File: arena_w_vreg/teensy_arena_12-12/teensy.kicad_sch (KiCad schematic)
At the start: 1 part, among them U13 Teensy4.1

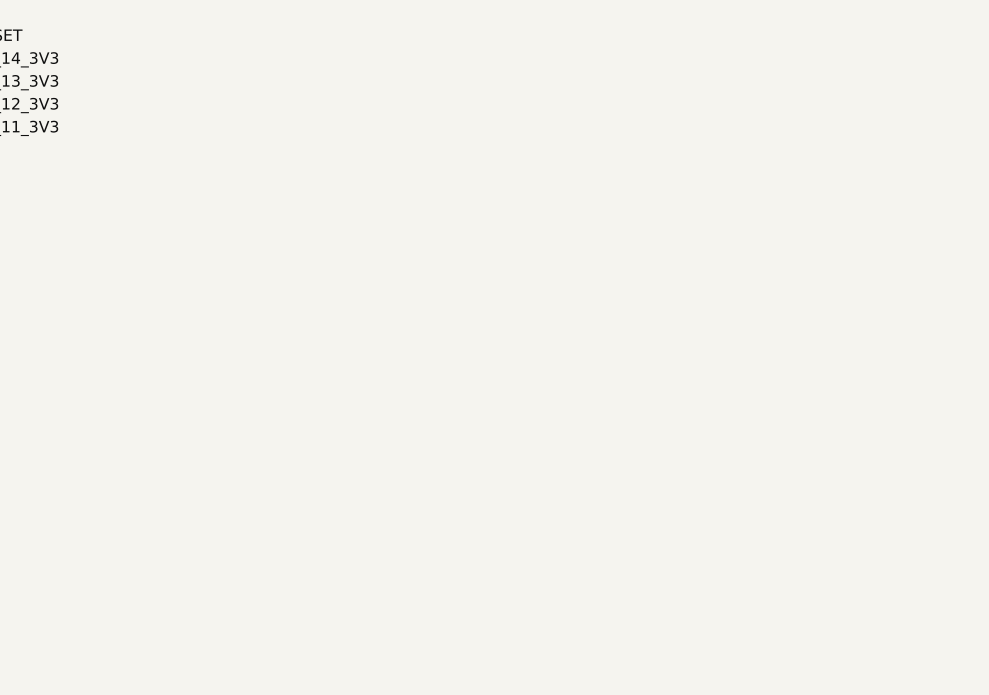
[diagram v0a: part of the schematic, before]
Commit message: Worked on 12-12 teensy arena with voltage regulator.
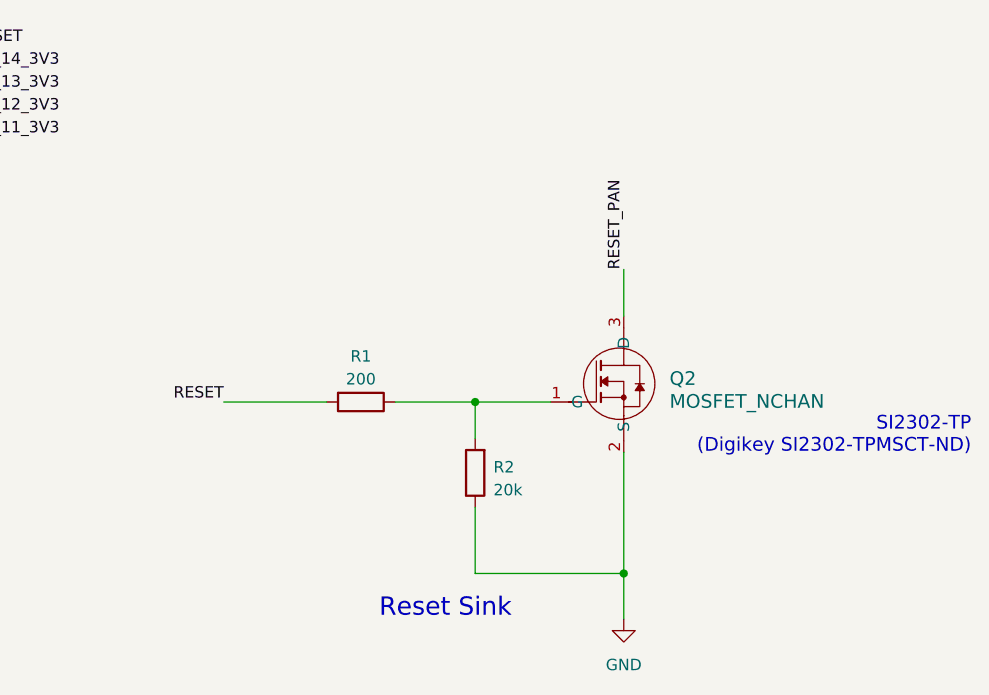
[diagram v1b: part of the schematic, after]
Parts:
- added Q2: MOSFET_NCHAN, Package_TO_SOT_SMD:SOT-23-3, symbol arena_custom:MOSFET_NCHAN
- added R1: 200, Resistor_SMD:R_0805_2012Metric, symbol Device:R
- added R2: 20k, Resistor_SMD:R_0805_2012Metric, symbol Device:R
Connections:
- net GND: now also Q2.2 (S), R2.1
- net RESET: now also R1.2
- new net: Q2.1 (G), R1.1, R2.2
- new net RESET_PAN: Q2.3 (D)
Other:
- note added: "Reset Sink"
- note added: "SI2302-TP (Digikey SI2302-TPMSCT-ND)"
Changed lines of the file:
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@@
 (kicad_sch (version 20230121) (generator eeschema)
   (paper "A4")
+  (junction (at 241.427 145.923) (diameter 0) (color 0 0 0 0)
+  )
+  (junction (at 224.917 126.873) (diameter 0) (color 0 0 0 0)
+  )
   (no_connect (at 165.227 113.919))
   (no_connect (at 165.227 84.709))
@@
     (stroke (width 0) (type default))
   )
+  (wire (pts (xy 196.977 126.873) (xy 208.407 126.873))
+    (stroke (width 0) (type default))
+  )
+  (wire (pts (xy 224.917 145.923) (xy 241.427 145.923))
+    (stroke (width 0) (type default))
+  )
   (wire (pts (xy 105.537 51.689) (xy 109.347 51.689))
     (stroke (width 0) (type default))
@@
     (stroke (width 0) (type default))
   )
+  (wire (pts (xy 224.917 126.873) (xy 233.299 126.873))
+    (stroke (width 0) (type default))
+  )
   (wire (pts (xy 188.087 41.529) (xy 188.087 42.799))
     (stroke (width 0) (type default))
@@
     (stroke (width 0) (type default))
   )
+  (wire (pts (xy 241.427 145.923) (xy 241.427 151.003))
+    (stroke (width 0) (type default))
+  )
   (wire (pts (xy 165.227 56.769) (xy 169.037 56.769))
     (stroke (width 0) (type default))
@@
     (stroke (width 0) (type default))
   )
+  (wire (pts (xy 216.027 126.873) (xy 224.917 126.873))
+    (stroke (width 0) (type default))
+  )
   (wire (pts (xy 105.537 56.769) (xy 109.347 56.769))
     (stroke (width 0) (type default))
@@
     (stroke (width 0) (type default))
   )
+  (wire (pts (xy 241.427 117.348) (xy 241.427 112.141))
+    (stroke (width 0) (type default))
+  )
   (wire (pts (xy 105.537 49.149) (xy 109.347 49.149))
     (stroke (width 0) (type default))
   )
+  (wire (pts (xy 241.427 132.461) (xy 241.427 145.923))
+    (stroke (width 0) (type default))
+  )
   (wire (pts (xy 105.537 92.329) (xy 109.347 92.329))
     (stroke (width 0) (type default))
@@
     (stroke (width 0) (type default))
   )
+  (wire (pts (xy 224.917 126.873) (xy 224.917 130.937))
+    (stroke (width 0) (type default))
+  )
   (wire (pts (xy 165.227 35.179) (xy 169.037 35.179))
     (stroke (width 0) (type default))
@@
     (stroke (width 0) (type default))
   )
+  (wire (pts (xy 224.917 138.557) (xy 224.917 145.923))
+    (stroke (width 0) (type default))
+  )
   (wire (pts (xy 105.537 97.409) (xy 109.347 97.409))
     (stroke (width 0) (type default))
@@
     (stroke (width 0) (type default))
   )
+  (text "Reset Sink" (at 214.249 151.003 0)
+    (effects (font (size 2.032 2.032)) (justify left bottom))
+  )
+  (text "SI2302-TP \n(Digikey SI2302-TPMSCT-ND)" (at 280.035 132.715 0)
+    (effects (font (size 1.524 1.524)) (justify right bottom))
+  )
   (label "MOSI_1_3V3" (at 105.537 82.169 180) (fields_autoplaced)
     (effects (font (size 1.27 1.27)) (justify right bottom))
@@
     (effects (font (size 1.27 1.27)) (justify left bottom))
   )
+  (label "RESET" (at 196.977 126.873 180) (fields_autoplaced)
+    (effects (font (size 1.27 1.27)) (justify right bottom))
+  )
   (label "3V3" (at 169.037 44.069 0) (fields_autoplaced)
     (effects (font (size 1.27 1.27)) (justify left bottom))
   )
+  (label "RESET_PAN" (at 241.427 112.141 90) (fields_autoplaced)
+    (effects (font (size 1.27 1.27)) (justify left bottom))
+  )
   (label "RESET" (at 169.037 87.249 0) (fields_autoplaced)
     (effects (font (size 1.27 1.27)) (justify left bottom))
@@
   (label "CS_09_3V3" (at 105.537 94.869 180) (fields_autoplaced)
     (effects (font (size 1.27 1.27)) (justify right bottom))
+  )
+  (symbol (lib_id "Device:R") (at 224.917 134.747 180) (unit 1)
+    (in_bom yes) (on_board yes) (dnp no) (fields_autoplaced)
+    (property "Reference" "R2" (at 226.949 134.112 0)
+      (effects (font (size 1.27 1.27)) (justify right))
+    )
+    (property "Value" "20k" (at 226.949 136.652 0)
+      (effects (font (size 1.27 1.27)) (justify right))
+    )
+    (property "Footprint" "Resistor_SMD:R_0805_2012Metric" (at 226.695 134.747 90)
+      (effects (font (size 1.27 1.27)) hide)
+    )
+    (property "Datasheet" "~" (at 224.917 134.747 0)
+      (effects (font (size 1.27 1.27)) hide)
+    )
+    (pin "1")
+    (pin "2")
+    (instances
+      (project "teensy_arena_12-12"
+        (path "/a2511654-3a17-43f1-8b9e-c45e375533dc"
+          (reference "R2") (unit 1)
+        )
+        (path "/a2511654-3a17-43f1-8b9e-c45e375533dc/5b6d0be6-08d3-404a-9e9b-565c640343d3"
+          (reference "R2") (unit 1)
+        )
+      )
+    )
   )
   (symbol (lib_id "arena_custom:Teensy4.1") (at 137.287 93.599 0) (unit 1)
@@
         )
       )
+    )
+  )
+  (symbol (lib_id "arena_custom:MOSFET_NCHAN") (at 241.427 126.873 0) (unit 1)
+    (in_bom yes) (on_board yes) (dnp no) (fields_autoplaced)
+    (property "Reference" "Q2" (at 246.507 124.2695 0)
+      (effects (font (size 1.524 1.524)) (justify left))
+    )
+    (property "Value" "MOSFET_NCHAN" (at 246.507 126.8095 0)
+      (effects (font (size 1.524 1.524)) (justify left))
+    )
+    (property "Footprint" "Package_TO_SOT_SMD:SOT-23-3" (at 241.427 124.587 0)
+      (effects (font (size 1.524 1.524)) hide)
+    )
+    (property "Datasheet" "" (at 241.427 124.587 0)
+      (effects (font (size 1.524 1.524)))
+    )
+    (pin "1")
+    (pin "2")
+    (pin "3")
+    (instances
+      (project "teensy_arena_12-12"
+        (path "/a2511654-3a17-43f1-8b9e-c45e375533dc"
+          (reference "Q2") (unit 1)
+        )
+        (path "/a2511654-3a17-43f1-8b9e-c45e375533dc/5b6d0be6-08d3-404a-9e9b-565c640343d3"
+          (reference "Q2") (unit 1)
+        )
+      )
+    )
+  )
+  (symbol (lib_id "Device:R") (at 212.217 126.873 270) (unit 1)
+    (in_bom yes) (on_board yes) (dnp no) (fields_autoplaced)
+    (property "Reference" "R1" (at 212.217 121.793 90)
+      (effects (font (size 1.27 1.27)))
+    )
+    (property "Value" "200" (at 212.217 124.333 90)
+      (effects (font (size 1.27 1.27)))
+    )
+    (property "Footprint" "Resistor_SMD:R_0805_2012Metric" (at 212.217 125.095 90)
+      (effects (font (size 1.27 1.27)) hide)
+    )
+    (property "Datasheet" "~" (at 212.217 126.873 0)
+      (effects (font (size 1.27 1.27)) hide)
+    )
+    (pin "1")
+    (pin "2")
+    (instances
+      (project "teensy_arena_12-12"
+        (path "/a2511654-3a17-43f1-8b9e-c45e375533dc"
+          (reference "R1") (unit 1)
+        )
+        (path "/a2511654-3a17-43f1-8b9e-c45e375533dc/5b6d0be6-08d3-404a-9e9b-565c640343d3"
+          (reference "R1") (unit 1)
+        )
+      )
+    )
+  )
+  (symbol (lib_id "power:GND") (at 241.427 151.003 0) (unit 1)
+    (in_bom yes) (on_board yes) (dnp no) (fields_autoplaced)
+    (property "Reference" "#PWR035" (at 241.427 157.353 0)
+      (effects (font (size 1.27 1.27)) hide)
+    )
+    (property "Value" "GND" (at 241.427 156.083 0)
+      (effects (font (size 1.27 1.27)))
+    )
+    (property "Footprint" "" (at 241.427 151.003 0)
+      (effects (font (size 1.27 1.27)) hide)
+    )
+    (property "Datasheet" "" (at 241.427 151.003 0)
+      (effects (font (size 1.27 1.27)) hide)
+    )
+    (pin "1")
+    (instances
+      (project "teensy_arena_12-12"
+        (path "/a2511654-3a17-43f1-8b9e-c45e375533dc"
+          (reference "#PWR035") (unit 1)
+        )
+        (path "/a2511654-3a17-43f1-8b9e-c45e375533dc/5b6d0be6-08d3-404a-9e9b-565c640343d3"
+          (reference "#PWR035") (unit 1)
+        )
+      )

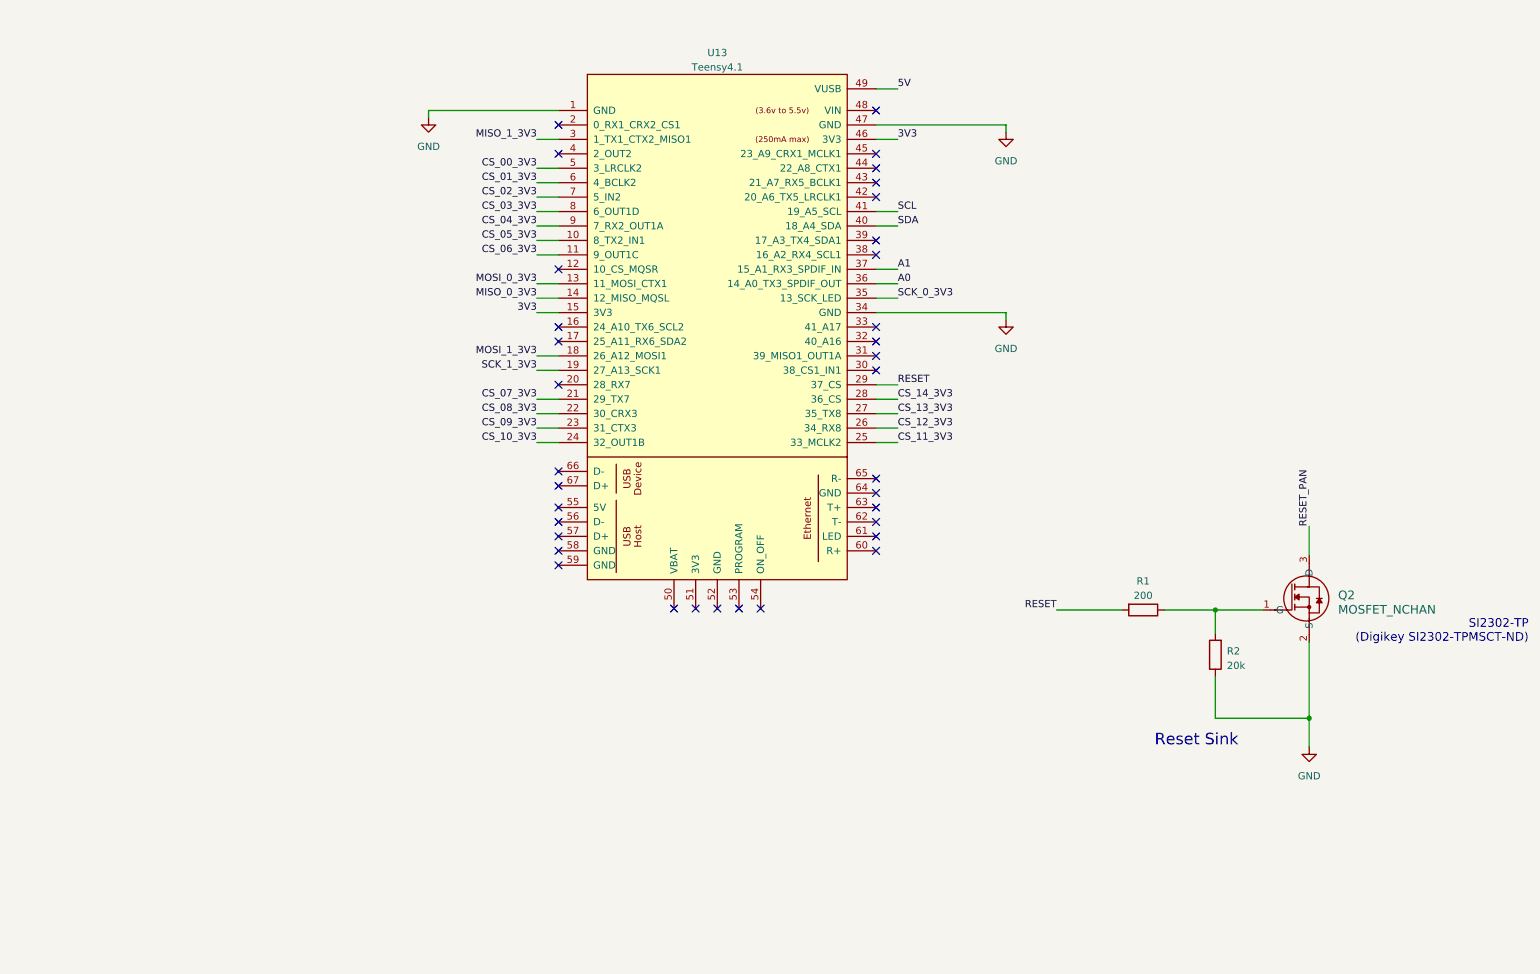
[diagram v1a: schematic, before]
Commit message: Worked on 12-12 teensy arean with voltage regulators.
Moved MOSFET to panel headers sheet. Added RESET to level sifters. Added
decouple caps for TXB0108's.
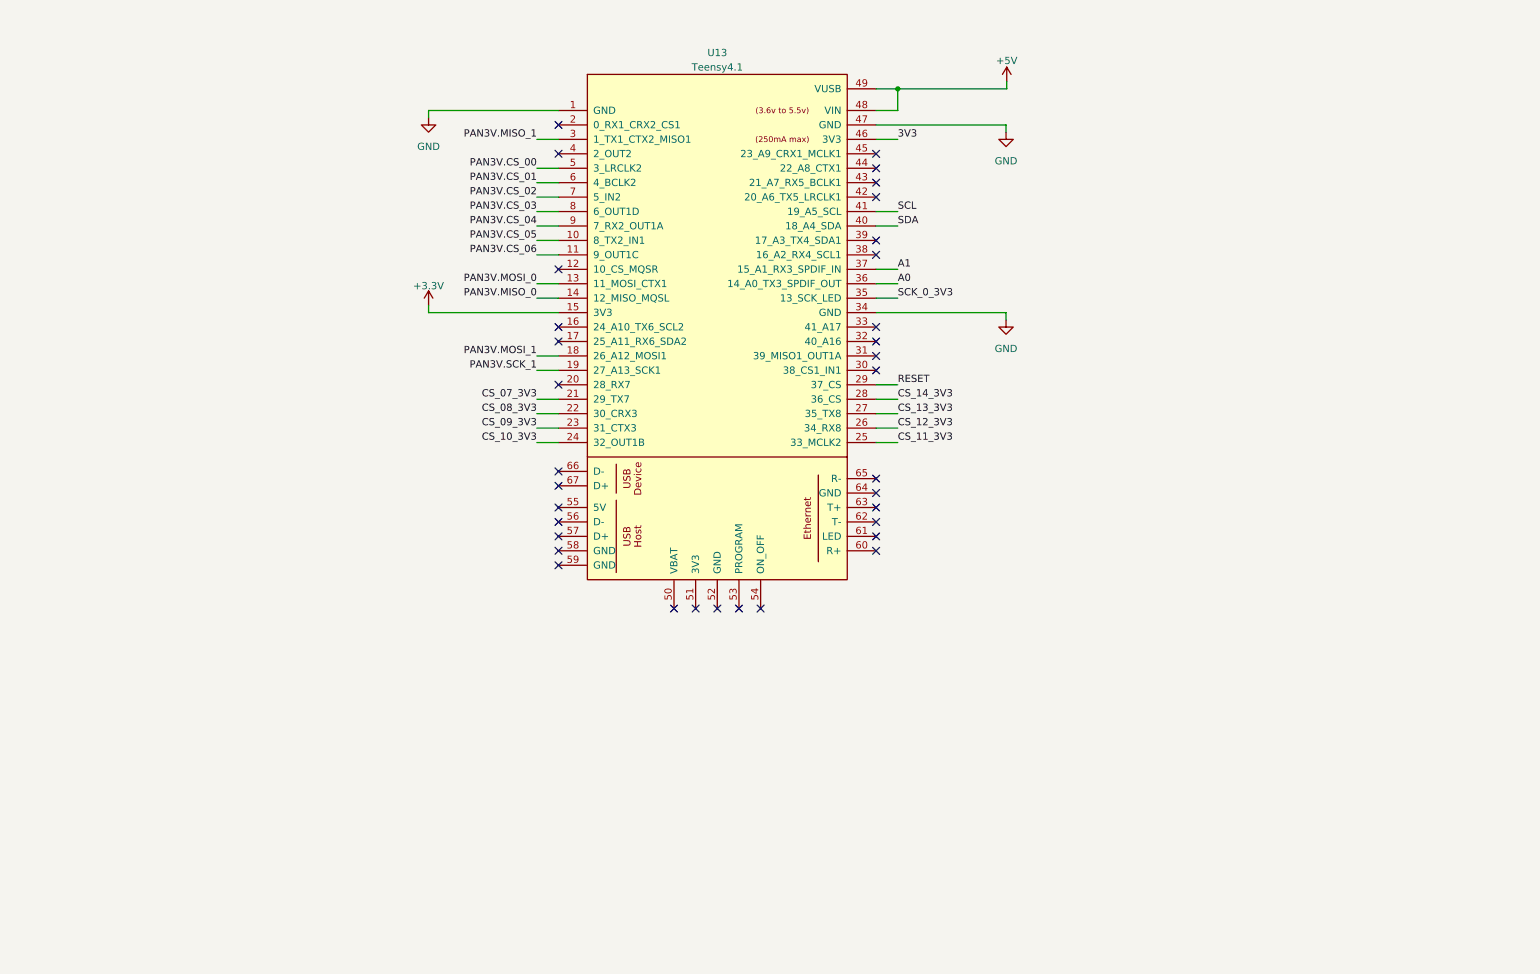
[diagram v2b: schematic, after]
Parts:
- removed Q2: MOSFET_NCHAN, Package_TO_SOT_SMD:SOT-23-3, symbol arena_custom:MOSFET_NCHAN
- removed R1: 200, Resistor_SMD:R_0805_2012Metric, symbol Device:R
- removed R2: 20k, Resistor_SMD:R_0805_2012Metric, symbol Device:R
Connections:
- net 5V is gone; now on net +5V: U13.49 (VUSB)
- net 3V3: no longer U13.15 (3V3)
- net +5V: now reaches U13.48 (VIN)
- net CS_00_3V3 renamed PAN3V.CS_00
- net CS_01_3V3 renamed PAN3V.CS_01
- net CS_02_3V3 renamed PAN3V.CS_02
- net CS_03_3V3 renamed PAN3V.CS_03
- net CS_04_3V3 renamed PAN3V.CS_04
- net CS_05_3V3 renamed PAN3V.CS_05
- net CS_06_3V3 renamed PAN3V.CS_06
- net MISO_0_3V3 renamed PAN3V.MISO_0
- net MISO_1_3V3 renamed PAN3V.MISO_1
- net MOSI_0_3V3 renamed PAN3V.MOSI_0
- net MOSI_1_3V3 renamed PAN3V.MOSI_1
- net SCK_1_3V3 renamed PAN3V.SCK_1
- new net +3.3V: U13.15 (3V3)
- no-connect marks 35 -> 34
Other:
- note removed: "Reset Sink"
- note removed: "SI2302-TP (Digikey SI2302-TPMSCT-ND)"
